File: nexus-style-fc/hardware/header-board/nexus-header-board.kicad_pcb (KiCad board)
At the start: 2 copper layers, 22.4 x 11 mm, 12 parts, among them J1 Servo header 3x7, K1 GND strip, K2 VX strip, P1 S1 tab pad, P2 S2 tab pad, P3 S3 tab pad, P4 TAIL tab pad, P5 ESC tab pad, P6 RPM tab pad, P7 SBUS tab pad, T1 GND tab pad, T2 VX tab pad

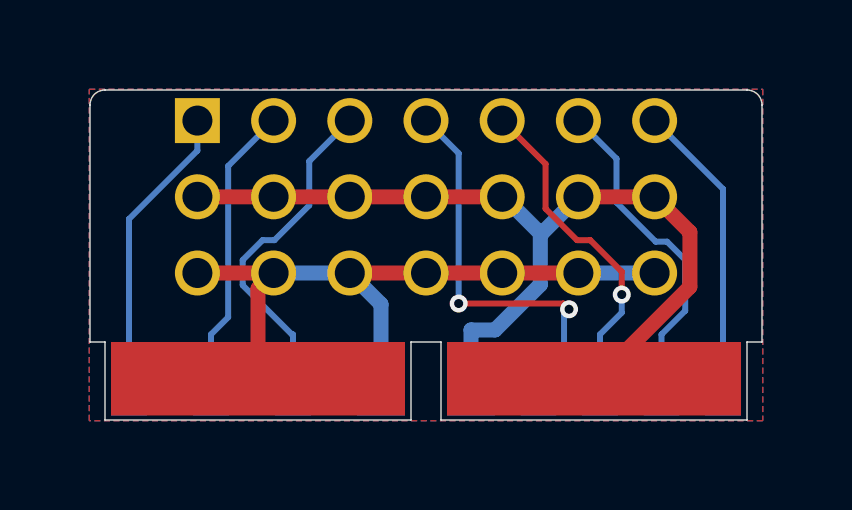
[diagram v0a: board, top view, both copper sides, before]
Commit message: Consolidate Nexus stage36 into canonical project paths
Preserve matched native sources and manufacturing bytes; use Git history for older project snapshots. Retain revision-bound validation evidence, document open release gates, and guard destructive regeneration.
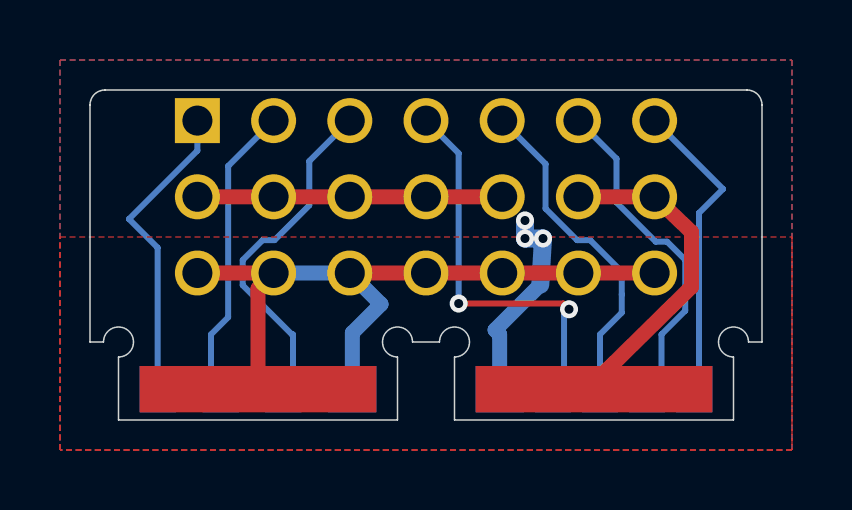
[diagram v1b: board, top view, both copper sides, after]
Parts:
- K1, K2: footprint NexusFC:ChildBoard_TabStrip_W9.8 -> NexusFC:ChildBoard_TabStrip_W7.892
- moved P1 0.95 mm to (102.3, 108.4)
- moved T1 0.95 mm to (108.7, 108.4)
- moved P7 0.95 mm to (120.1, 108.4)
- moved T2 0.95 mm to (113.7, 108.4)
- moved P4 0.48 mm to (115.4, 108.4)
- moved P6 0.48 mm to (118.6, 108.4)
- moved P2 0.32 mm to (104.4, 108.4)
- moved P3 0.32 mm to (106.4, 108.4)
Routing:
- net VX: track 30.5 -> 27.2 mm, vias 0 -> 3
- net ESC: vias 1 -> 0
- added copper zone on F.Cu, net VX
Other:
- outline, holes or cut-outs redrawn

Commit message: improved child board
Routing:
- net VX: vias 3 -> 19
- net GND: vias 0 -> 11
- added copper zone on In2.Cu, net GND
- added copper zone on B.Cu, net VX
- added copper zone on In1.Cu, net VX
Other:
- copper layers 2 -> 4

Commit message: updated bom
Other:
- outline, holes or cut-outs redrawn
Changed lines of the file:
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@@
 		(pad "1" thru_hole rect
 			(at -7.62 -2.54)
-			(size 1.5 1.5)
+			(size 1.52 1.52)
 			(drill 1)
 			(layers "*.Cu" "*.Mask")
@@
 		(pad "2" thru_hole circle
 			(at -7.62 0)
-			(size 1.5 1.5)
+			(size 1.52 1.52)
 			(drill 1)
 			(layers "*.Cu" "*.Mask")
@@
 		(pad "3" thru_hole circle
 			(at -7.62 2.54)
-			(size 1.5 1.5)
+			(size 1.52 1.52)
 			(drill 1)
 			(layers "*.Cu" "*.Mask")
@@
 		(pad "4" thru_hole circle
 			(at -5.08 -2.54)
-			(size 1.5 1.5)
+			(size 1.52 1.52)
 			(drill 1)
 			(layers "*.Cu" "*.Mask")
@@
 		(pad "5" thru_hole circle
 			(at -5.08 0)
-			(size 1.5 1.5)
+			(size 1.52 1.52)
 			(drill 1)
 			(layers "*.Cu" "*.Mask")
@@
 		(pad "6" thru_hole circle
 			(at -5.08 2.54)
-			(size 1.5 1.5)
+			(size 1.52 1.52)
 			(drill 1)
 			(layers "*.Cu" "*.Mask")
@@
 		(pad "7" thru_hole circle
 			(at -2.54 -2.54)
-			(size 1.5 1.5)
+			(size 1.52 1.52)
 			(drill 1)
 			(layers "*.Cu" "*.Mask")
@@
 		(pad "8" thru_hole circle
 			(at -2.54 0)
-			(size 1.5 1.5)
+			(size 1.52 1.52)
 			(drill 1)
 			(layers "*.Cu" "*.Mask")
@@
 		(pad "9" thru_hole circle
 			(at -2.54 2.54)
-			(size 1.5 1.5)
+			(size 1.52 1.52)
 			(drill 1)
 			(layers "*.Cu" "*.Mask")
@@
 		(pad "10" thru_hole circle
 			(at 0 -2.54)
-			(size 1.5 1.5)
+			(size 1.52 1.52)
 			(drill 1)
 			(layers "*.Cu" "*.Mask")
@@
 		(pad "11" thru_hole circle
 			(at 0 0)
-			(size 1.5 1.5)
+			(size 1.52 1.52)
 			(drill 1)
 			(layers "*.Cu" "*.Mask")
@@
 		(pad "12" thru_hole circle
 			(at 0 2.54)
-			(size 1.5 1.5)
+			(size 1.52 1.52)
 			(drill 1)
 			(layers "*.Cu" "*.Mask")
@@
 		(pad "13" thru_hole circle
 			(at 2.54 -2.54)
-			(size 1.5 1.5)
+			(size 1.52 1.52)
 			(drill 1)
 			(layers "*.Cu" "*.Mask")
@@
 		(pad "14" thru_hole circle
 			(at 2.54 0)
-			(size 1.5 1.5)
+			(size 1.52 1.52)
 			(drill 1)
 			(layers "*.Cu" "*.Mask")
@@
 		(pad "15" thru_hole circle
 			(at 2.54 2.54)
-			(size 1.5 1.5)
+			(size 1.52 1.52)
 			(drill 1)
 			(layers "*.Cu" "*.Mask")
@@
 		(pad "16" thru_hole circle
 			(at 5.08 -2.54)
-			(size 1.5 1.5)
+			(size 1.52 1.52)
 			(drill 1)
 			(layers "*.Cu" "*.Mask")
@@
 		(pad "17" thru_hole circle
 			(at 5.08 0)
-			(size 1.5 1.5)
+			(size 1.52 1.52)
 			(drill 1)
 			(layers "*.Cu" "*.Mask")
@@
 		(pad "18" thru_hole circle
 			(at 5.08 2.54)
-			(size 1.5 1.5)
+			(size 1.52 1.52)
 			(drill 1)
 			(layers "*.Cu" "*.Mask")
@@
 		(pad "19" thru_hole circle
 			(at 7.62 -2.54)
-			(size 1.5 1.5)
+			(size 1.52 1.52)
 			(drill 1)
 			(layers "*.Cu" "*.Mask")
@@
 		(pad "20" thru_hole circle
 			(at 7.62 0)
-			(size 1.5 1.5)
+			(size 1.52 1.52)
 			(drill 1)
 			(layers "*.Cu" "*.Mask")
@@
 		(pad "21" thru_hole circle
 			(at 7.62 2.54)
-			(size 1.5 1.5)
+			(size 1.52 1.52)
 			(drill 1)
 			(layers "*.Cu" "*.Mask")
@@
 	(gr_line
 		(start 100 108.4)
-		(end 100.45 108.4)
-		(stroke
-			(width 0.05)
-			(type solid)
-		)
-		(layer "Edge.Cuts")
-	)
-	(gr_arc
-		(start 100.45 108.4)
-		(mid 100.95 107.9)
-		(end 101.45 108.4)
+		(end 100.9 108.4)
 		(stroke
 			(width 0.05)
@@
 		(layer "Edge.Cuts")
 	)
+	(gr_arc
+		(start 100.9 108.4)
+		(mid 101.4 107.9)
+		(end 101.9 108.4)
+		(stroke
+			(width 0.05)
+			(type solid)
+		)
+		(layer "Edge.Cuts")
+	)
 	(gr_line
-		(start 100.95 108.9)
-		(end 100.95 111)
+		(start 101.4 108.9)
+		(end 101.4 111)
 		(stroke
 			(width 0.05)
@@
 	)
 	(gr_line
-		(start 100.95 111)
-		(end 110.25 111)
+		(start 101.4 111)
+		(end 109.8 111)
 		(stroke
 			(width 0.05)
@@
 	)
 	(gr_arc
-		(start 101.45 108.4)
-		(mid 101.303553 108.753553)
-		(end 100.95 108.9)
+		(start 101.9 108.4)
+		(mid 101.753553 108.753553)
+		(end 101.4 108.9)
 		(stroke
 			(width 0.05)
@@
 	)
 	(gr_arc
-		(start 109.75 108.4)
-		(mid 110.25 107.9)
-		(end 110.75 108.4)
+		(start 109.3 108.4)
+		(mid 109.8 107.9)
+		(end 110.3 108.4)
 		(stroke
 			(width 0.05)
@@
 	)
 	(gr_arc
-		(start 110.25 108.9)
-		(mid 109.896447 108.753553)
-		(end 109.75 108.4)
+		(start 109.8 108.9)
+		(mid 109.446447 108.753553)
+		(end 109.3 108.4)
 		(stroke
 			(width 0.05)
@@
 	)
 	(gr_line
-		(start 110.25 111)
-		(end 110.25 108.9)
+		(start 109.8 111)
+		(end 109.8 108.9)
 		(stroke
 			(width 0.05)
@@
 	)
 	(gr_line
-		(start 110.75 108.4)
-		(end 111.65 108.4)
+		(start 110.3 108.4)
+		(end 112.1 108.4)
 		(stroke
 			(width 0.05)
@@
 	)
 	(gr_arc
-		(start 111.65 108.4)
-		(mid 112.15 107.9)
-		(end 112.65 108.4)
+		(start 112.1 108.4)
+		(mid 112.6 107.9)
+		(end 113.1 108.4)
 		(stroke
 			(width 0.05)
@@
 	)
 	(gr_line
-		(start 112.15 108.9)
-		(end 112.15 111)
+		(start 112.6 108.9)
+		(end 112.6 111)
 		(stroke
 			(width 0.05)
@@
 	)
 	(gr_line
-		(start 112.15 111)
-		(end 121.45 111)
+		(start 112.6 111)
+		(end 121 111)
 		(stroke
 			(width 0.05)
@@
 	)
 	(gr_arc
-		(start 112.65 108.4)
-		(mid 112.503553 108.753553)
-		(end 112.15 108.9)
+		(start 113.1 108.4)
+		(mid 112.953553 108.753553)
+		(end 112.6 108.9)
 		(stroke
 			(width 0.05)
@@
 	)
 	(gr_arc
-		(start 120.95 108.4)
-		(mid 121.45 107.9)
-		(end 121.95 108.4)
+		(start 120.5 108.4)
+		(mid 121 107.9)
+		(end 121.5 108.4)
 		(stroke
 			(width 0.05)
@@
 	)
 	(gr_arc
-		(start 121.45 108.9)
-		(mid 121.096447 108.753553)
-		(end 120.95 108.4)
+		(start 121 108.9)
+		(mid 120.646447 108.753553)
+		(end 120.5 108.4)
 		(stroke
 			(width 0.05)
@@
 	)
 	(gr_line
-		(start 121.45 111)
-		(end 121.45 108.9)
+		(start 121 111)
+		(end 121 108.9)
+		(stroke
+			(width 0.05)
+			(type solid)
+		)
+		(layer "Edge.Cuts")
+	)
+	(gr_line
+		(start 121.5 108.4)
+		(end 122.4 108.4)
 		(stroke
 			(width 0.05)
@@
 			(width 0.05)
 			(type default)
-		)
-		(layer "Edge.Cuts")
-	)
-	(gr_line
-		(start 121.95 108.4)
-		(end 122.4 108.4)
-		(stroke
-			(width 0.05)
-			(type solid)
 		)
 		(layer "Edge.Cuts")
@@
 	)
 	(segment
-		(start 113.5022 107.9983)
+		(start 113.54 107.94)
 		(end 113.654 108.1501)
 		(width 0.5)
@@
 	(segment
 		(start 115.01 106.4905)
-		(end 113.5022 107.9983)
+		(end 113.54 107.94)
 		(width 0.5)
 		(layer "B.Cu")
@@
 	)
 	(segment
+		(start 120.1 107.8695)
+		(end 120.1 109.28)
+		(width 0.2)
+		(layer "B.Cu")
+		(net "SBUS")
+	)
+	(segment
 		(start 120.4695 102.6695)
-		(end 120.4695 109.6495)
+		(end 120.4695 107.5)
+		(width 0.2)
+		(layer "B.Cu")
+		(net "SBUS")
+	)
+	(segment
+		(start 120.4695 107.5)
+		(end 120.1 107.8695)
 		(width 0.2)
 		(layer "B.Cu")
@@
 	)
 	(segment
+		(start 120.1 109.28)
+		(end 120.4695 109.6495)
+		(width 0.2)
+		(layer "B.Cu")
+		(net "SBUS")
+	)
+	(segment
 		(start 103.58 101.02)
 		(end 103.58 102.0217)
@@
 	(segment
 		(start 115.7775 107.1179)
+		(end 115.6775 107.1279)
+		(width 0.2)
+		(layer "F.Cu")
+		(net "TAIL")
+	)
+	(segment
+		(start 115.6775 107.1279)
+		(end 112.3888 107.1279)
+		(width 0.2)
+		(layer "F.Cu")
+		(net "TAIL")
+	)
+	(segment
+		(start 112.3888 107.1279)
 		(end 112.2888 107.1179)
 		(width 0.2)
@@
 	(segment
 		(start 108.66 106.1)
-		(end 109.7 107.14)
-		(width 0.5)
-		(layer "B.Cu")
-		(net "GND")
-	)
-	(segment
-		(start 109.7 107.14)
+		(end 109.6 107.04)
+		(width 0.5)
+		(layer "B.Cu")
+		(net "GND")
+	)
+	(segment
+		(start 109.6 107.04)
 		(end 108.746 108.094)
 		(width 0.5)
@@
 	(segment
 		(start 105.0902 105.6685)
-		(end 105.0902 106.5086)
+		(end 105.0802 106.5086)
 		(width 0.2)
 		(layer "B.Cu")
@@
 	)
 	(segment
-		(start 105.0902 106.5086)
+		(start 105.0802 106.5086)
 		(end 106.7299 108.1483)
 		(width 0.2)
